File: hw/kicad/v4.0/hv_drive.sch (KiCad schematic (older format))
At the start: 24 parts, among them P6 CONN_01X02, P8 CONN_01X03, U12 IRAM256a

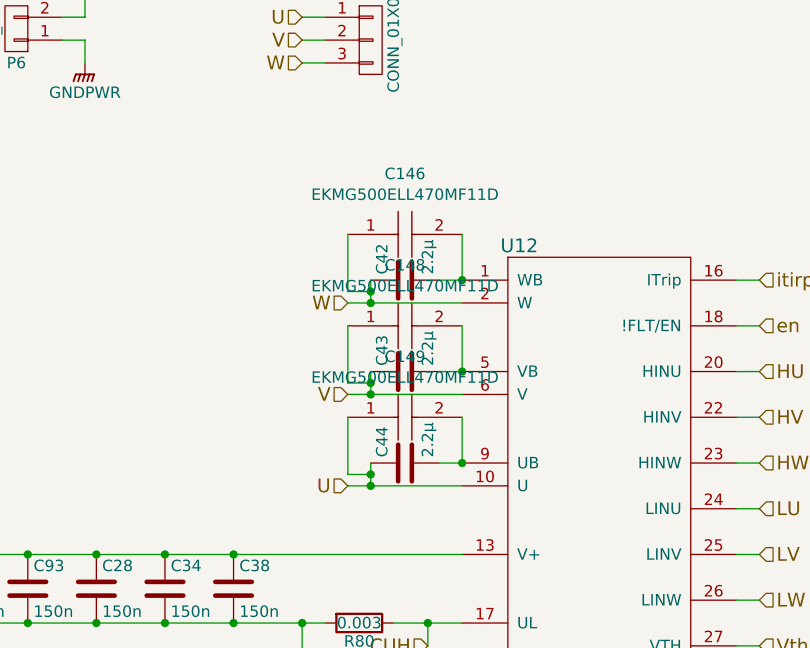
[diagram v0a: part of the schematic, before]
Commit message: added IKCM30F60GD
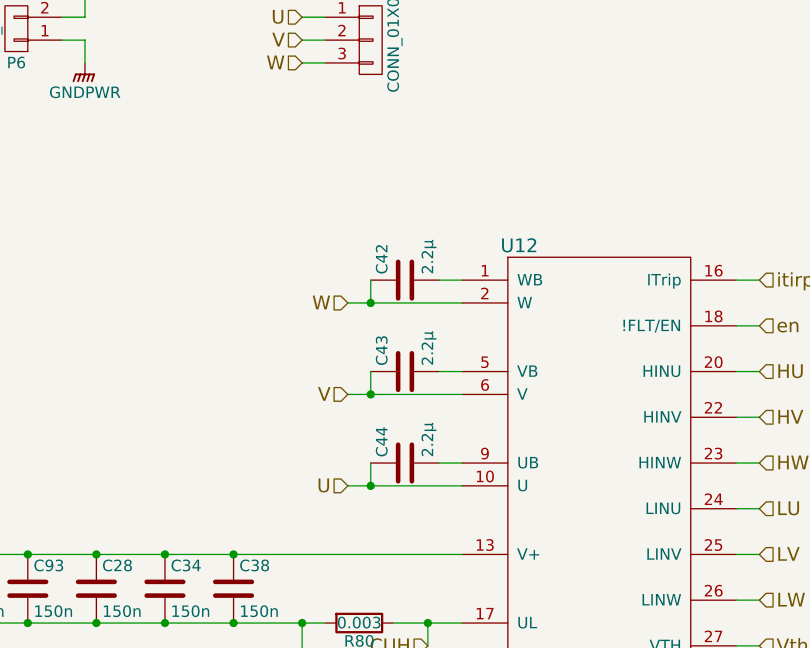
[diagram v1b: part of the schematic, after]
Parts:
- removed C146, C148, C149: EKMG500ELL470MF11D, SamacSys_Parts:CAPPRD250W60D680H1250, symbol SamacSys_Parts:EKMG500ELL470MF11D
- C42, C43, C44: footprint stmbl:C_1206 -> stmbl:C_0603
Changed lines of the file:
@@
 EESchema Schematic File Version 4
-EELAYER 30 0
+LIBS:stmbl_4.0-cache
+EELAYER 26 0
 EELAYER END
 $Descr A4 11693 8268
@@
 F 0 "C42" H 5625 3150 50  0000 L CNN
 F 1 "2.2µ" H 5625 2950 50  0000 L CNN
-F 2 "stmbl:C_1206" H 5638 2900 30  0001 C CNN
+F 2 "stmbl:C_0603" H 5638 2900 30  0001 C CNN
 F 3 "" H 5600 3050 60  0000 C CNN
 F 4 "" H 5600 3050 60  0001 C CNN "InternalName"
@@
 F 0 "C43" H 5625 3550 50  0000 L CNN
 F 1 "2.2µ" H 5625 3350 50  0000 L CNN
-F 2 "stmbl:C_1206" H 5638 3300 30  0001 C CNN
+F 2 "stmbl:C_0603" H 5638 3300 30  0001 C CNN
 F 3 "" H 5600 3450 60  0000 C CNN
 F 4 "" H 5600 3450 60  0001 C CNN "InternalName"
@@
 	5350 3550 5450 3550
 Wire Wire Line
-	5450 3450 5450 3500
+	5450 3450 5450 3550
 Connection ~ 5450 3550
 $Comp
@@
 F 0 "C44" H 5625 3950 50  0000 L CNN
 F 1 "2.2µ" H 5625 3750 50  0000 L CNN
-F 2 "stmbl:C_1206" H 5638 3700 30  0001 C CNN
+F 2 "stmbl:C_0603" H 5638 3700 30  0001 C CNN
 F 3 "" H 5600 3850 60  0000 C CNN
 F 4 "" H 5600 3850 60  0001 C CNN "InternalName"
@@
 $EndComp
 Wire Wire Line
+	5850 3850 5750 3850
+Wire Wire Line
 	5350 3950 5450 3950
 Wire Wire Line
-	5450 3850 5450 3900
+	5450 3850 5450 3950
 Connection ~ 5450 3950
 $Comp
@@
 	7800 4550 7900 4550
 Wire Wire Line
-	5450 3050 5450 3100
+	5450 3050 5450 3150
 Wire Wire Line
 	5150 4550 5150 4750
@@
 Wire Wire Line
 	8100 4750 8400 4750
-$Comp
-L SamacSys_Parts:EKMG500ELL470MF11D C146
-U 1 1 5DF898C9
-P 5350 2850
-F 0 "C146" H 5600 3115 50  0000 C CNN
-F 1 "EKMG500ELL470MF11D" H 5600 3024 50  0000 C CNN
-F 2 "SamacSys_Parts:CAPPRD250W60D680H1250" H 5700 2900 50  0001 L CNN
-F 3 "https://componentsearchengine.com/Datasheets/1/EKMG500ELL470MF11D.pdf" H 5700 2800 50  0001 L CNN
-F 4 "UNITED CHEMI-CON - EKMG500ELL470MF11D - ALUMINUM ELECTROLYTIC CAPACITOR 47UF, 50V, 20%, RADIAL" H 5700 2700 50  0001 L CNN "Description"
-F 5 "12.5" H 5700 2600 50  0001 L CNN "Height"
-F 6 "661-EKMGG500ELL470MF" H 5700 2500 50  0001 L CNN "Mouser Part Number"
-F 7 "https://www.mouser.com/Search/Refine.aspx?Keyword=661-EKMGG500ELL470MF" H 5700 2400 50  0001 L CNN "Mouser Price/Stock"
-F 8 "United Chemi-Con" H 5700 2300 50  0001 L CNN "Manufacturer_Name"
-F 9 "EKMG500ELL470MF11D" H 5700 2200 50  0001 L CNN "Manufacturer_Part_Number"
-	1    5350 2850
-	1    0    0    -1
-$EndComp
-$Comp
-L SamacSys_Parts:EKMG500ELL470MF11D C148
-U 1 1 5DF8F912
-P 5350 3250
-F 0 "C148" H 5600 3515 50  0000 C CNN
-F 1 "EKMG500ELL470MF11D" H 5600 3424 50  0000 C CNN
-F 2 "SamacSys_Parts:CAPPRD250W60D680H1250" H 5700 3300 50  0001 L CNN
-F 3 "https://componentsearchengine.com/Datasheets/1/EKMG500ELL470MF11D.pdf" H 5700 3200 50  0001 L CNN
-F 4 "UNITED CHEMI-CON - EKMG500ELL470MF11D - ALUMINUM ELECTROLYTIC CAPACITOR 47UF, 50V, 20%, RADIAL" H 5700 3100 50  0001 L CNN "Description"
-F 5 "12.5" H 5700 3000 50  0001 L CNN "Height"
-F 6 "661-EKMGG500ELL470MF" H 5700 2900 50  0001 L CNN "Mouser Part Number"
-F 7 "https://www.mouser.com/Search/Refine.aspx?Keyword=661-EKMGG500ELL470MF" H 5700 2800 50  0001 L CNN "Mouser Price/Stock"
-F 8 "United Chemi-Con" H 5700 2700 50  0001 L CNN "Manufacturer_Name"
-F 9 "EKMG500ELL470MF11D" H 5700 2600 50  0001 L CNN "Manufacturer_Part_Number"
-	1    5350 3250
-	1    0    0    -1
-$EndComp
-$Comp
-L SamacSys_Parts:EKMG500ELL470MF11D C149
-U 1 1 5DF91ED9
-P 5350 3650
-F 0 "C149" H 5600 3915 50  0000 C CNN
-F 1 "EKMG500ELL470MF11D" H 5600 3824 50  0000 C CNN
-F 2 "SamacSys_Parts:CAPPRD250W60D680H1250" H 5700 3700 50  0001 L CNN
-F 3 "https://componentsearchengine.com/Datasheets/1/EKMG500ELL470MF11D.pdf" H 5700 3600 50  0001 L CNN
-F 4 "UNITED CHEMI-CON - EKMG500ELL470MF11D - ALUMINUM ELECTROLYTIC CAPACITOR 47UF, 50V, 20%, RADIAL" H 5700 3500 50  0001 L CNN "Description"
-F 5 "12.5" H 5700 3400 50  0001 L CNN "Height"
-F 6 "661-EKMGG500ELL470MF" H 5700 3300 50  0001 L CNN "Mouser Part Number"
-F 7 "https://www.mouser.com/Search/Refine.aspx?Keyword=661-EKMGG500ELL470MF" H 5700 3200 50  0001 L CNN "Mouser Price/Stock"
-F 8 "United Chemi-Con" H 5700 3100 50  0001 L CNN "Manufacturer_Name"
-F 9 "EKMG500ELL470MF11D" H 5700 3000 50  0001 L CNN "Manufacturer_Part_Number"
-	1    5350 3650
-	1    0    0    -1
-$EndComp
-Wire Wire Line
-	5850 3650 5850 3850
-Connection ~ 5850 3850
-Wire Wire Line
-	5850 3250 5850 3450
-Wire Wire Line
-	5750 3850 5850 3850
-Connection ~ 5850 3450
-Wire Wire Line
-	5850 2850 5850 3050
-Connection ~ 5850 3050
-Wire Wire Line
-	5350 2850 5350 3100
-Wire Wire Line
-	5350 3100 5450 3100
-Connection ~ 5450 3100
-Wire Wire Line
-	5450 3100 5450 3150
-Wire Wire Line
-	5350 3250 5350 3500
-Wire Wire Line
-	5350 3500 5450 3500
-Connection ~ 5450 3500
-Wire Wire Line
-	5450 3500 5450 3550
-Wire Wire Line
-	5350 3650 5350 3900
-Wire Wire Line
-	5350 3900 5450 3900
-Connection ~ 5450 3900
-Wire Wire Line
-	5450 3900 5450 3950
 $EndSCHEMATC

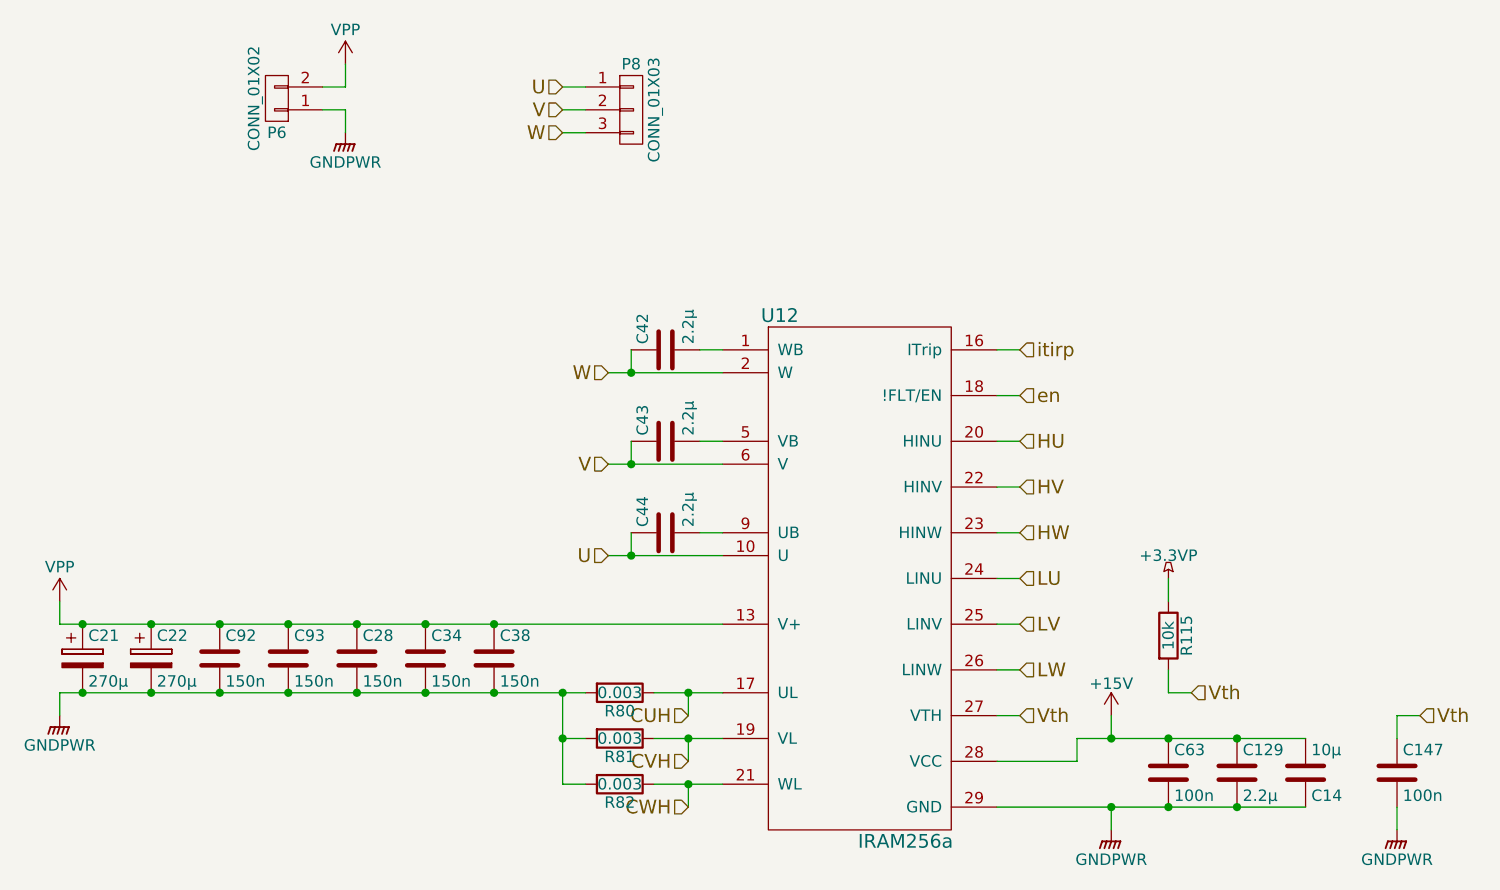
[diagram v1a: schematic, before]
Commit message: schematic update
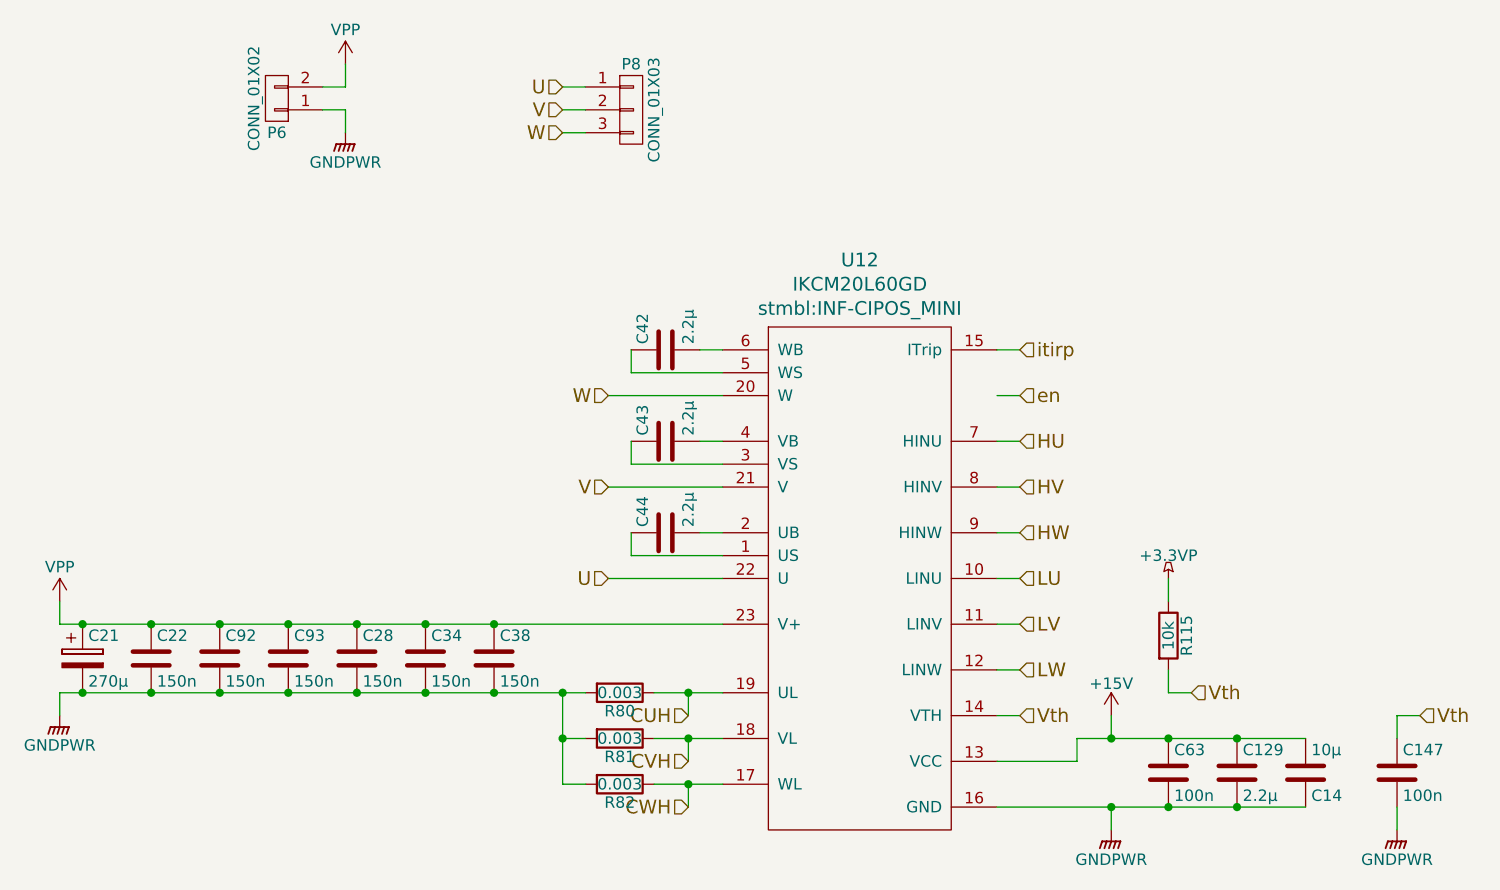
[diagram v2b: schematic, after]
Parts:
- removed C22: 270µ, stmbl:C_Radial_D26_L45_P10, symbol stmbl:CP
- removed U12: IRAM256a, stmbl:IRAM256, symbol stmbl:IRAM256a
- added C22: 150n, stmbl:C_1808, symbol stmbl:C
- added U12: IKCM20L60GD, stmbl:INF-CIPOS_MINI, symbol stmbl:IKCM20L60GD
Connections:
- net +15V: now also U12.13 (VCC)
- net CUH: now also U12.19 (UL)
- net CVH: now also U12.18 (VL)
- net CWH: now also U12.17 (WL)
- net GNDPWR: now also C22.2, U12.16 (GND)
- net HU: now also U12.7 (HINU)
- net HV: now also U12.8 (HINV)
- net HW: now also U12.9 (HINW)
- net LU: now also U12.10 (LINU)
- net LV: now also U12.11 (LINV)
- net LW: now also U12.12 (LINW)
- net U: now also U12.22 (U); no longer C44.1
- net V: now also U12.21 (V); no longer C43.1
- net VPP: now also C22.1, U12.23 (V+)
- net Vth: now also U12.14 (VTH)
- net W: now also U12.20 (W); no longer C42.1
- net itirp: now also U12.15 (ITrip)
- net at C42.2: now also U12.6 (WB)
- net at C43.2: now also U12.4 (VB)
- net at C44.2: now also U12.2 (UB)
- new net: C42.1, U12.5 (WS)
- new net: C43.1, U12.3 (VS)
- new net: C44.1, U12.1 (US)
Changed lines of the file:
@@
 EESchema Schematic File Version 4
-LIBS:stmbl_4.0-cache
-EELAYER 26 0
+EELAYER 30 0
 EELAYER END
 $Descr A4 11693 8268
@@
 $EndComp
 $Comp
-L stmbl:CP C22
-U 1 1 56590CD1
-P 3350 4400
-F 0 "C22" H 3375 4500 50  0000 L CNN
-F 1 "270µ" H 3375 4300 50  0000 L CNN
-F 2 "stmbl:C_Radial_D26_L45_P10" H 3388 4250 30  0001 C CNN
-F 3 "" H 3350 4400 60  0000 C CNN
-F 4 "" H 3350 4400 60  0001 C CNN "InternalName"
-F 5 "ESMR401VSN271MQ30S" H 3350 4400 60  0001 C CNN "Manufacturer No"
-F 6 "400V" H 3350 4400 60  0001 C CNN "Voltage"
-F 7 "" H 3350 4400 60  0001 C CNN "Source"
-F 8 "" H 3350 4400 60  0001 C CNN "Tolerance"
-F 9 "" H 0   0   50  0001 C CNN "Description"
-F 10 "United Chemi-Con" H 0   0   50  0001 C CNN "Manufacturer"
-	1    3350 4400
-	1    0    0    -1
-$EndComp
-$Comp
 L stmbl:C C28
 U 1 1 56590D2C
@@
 Connection ~ 4550 4550
 Connection ~ 4250 4550
-Connection ~ 3350 4550
-Connection ~ 3350 4250
 Connection ~ 4250 4250
 Connection ~ 4550 4250
@@
 Wire Wire Line
 	5850 3050 5750 3050
-Wire Wire Line
-	5350 3150 5450 3150
-Text HLabel 5350 3150 0    60   Input ~ 0
-W
-Text HLabel 5350 3550 0    60   Input ~ 0
-V
-Text HLabel 5350 3950 0    60   Input ~ 0
-U
 Connection ~ 3050 4250
-Connection ~ 5450 3150
 Text HLabel 5150 1900 0    60   Input ~ 0
 U
@@
 $EndComp
 $Comp
-L stmbl:IRAM256a U12
-U 1 1 5668DD3B
-P 6450 4050
-F 0 "U12" H 6100 5200 60  0000 C CNN
-F 1 "IRAM256a" H 6650 2900 60  0000 C CNN
-F 2 "stmbl:IRAM256" H 6450 4050 60  0001 C CNN
-F 3 "" H 6450 4050 60  0000 C CNN
-F 4 "IRAM256-2067A2" H 6450 4050 50  0001 C CNN "Manufacturer No"
-F 5 "" H 6450 4050 50  0001 C CNN "Voltage"
-F 6 "" H 6450 4050 50  0001 C CNN "Source"
-F 7 "" H 6450 4050 60  0001 C CNN "InternalName"
-F 8 "" H 6450 4050 60  0001 C CNN "Tolerance"
-F 9 "" H 0   0   50  0001 C CNN "Description"
-F 10 "Infineon" H 0   0   50  0001 C CNN "Manufacturer"
-	1    6450 4050
-	1    0    0    -1
-$EndComp
-$Comp
 L stmbl:C C43
 U 1 1 5668E03D
@@
 	5850 3450 5750 3450
 Wire Wire Line
-	5350 3550 5450 3550
-Wire Wire Line
 	5450 3450 5450 3550
-Connection ~ 5450 3550
 $Comp
 L stmbl:C C44
@@
 	5850 3850 5750 3850
 Wire Wire Line
-	5350 3950 5450 3950
-Wire Wire Line
 	5450 3850 5450 3950
-Connection ~ 5450 3950
 $Comp
 L stmbl:R R80
@@
 	4250 4550 4550 4550
 Wire Wire Line
+	4250 4250 4550 4250
+Wire Wire Line
+	4550 4250 4850 4250
+Wire Wire Line
+	5150 4550 5250 4550
+Wire Wire Line
+	5450 3150 5850 3150
+Wire Wire Line
+	5450 3550 5850 3550
+Wire Wire Line
+	5450 3950 5850 3950
+Wire Wire Line
+	5700 4550 5850 4550
+Wire Wire Line
+	5700 4750 5850 4750
+Wire Wire Line
+	5700 4950 5850 4950
+Wire Wire Line
+	7550 5050 7800 5050
+Wire Wire Line
+	7550 4750 7800 4750
+Wire Wire Line
+	5150 4750 5150 4950
+Wire Wire Line
+	3650 4550 3950 4550
+Wire Wire Line
+	3950 4550 4250 4550
+Wire Wire Line
+	3950 4250 4250 4250
+Wire Wire Line
+	3650 4250 3950 4250
+Wire Wire Line
+	4850 4550 5150 4550
+Wire Wire Line
+	4850 4250 5850 4250
+Wire Wire Line
+	7800 5050 8100 5050
+Wire Wire Line
+	7800 4750 8100 4750
+Wire Wire Line
+	8100 5050 8400 5050
+Wire Wire Line
+	8100 4750 8400 4750
+$Comp
+L stmbl:IKCM20L60GD U12
+U 1 1 5EC2EF5C
+P 6450 4050
+F 0 "U12" H 6450 5443 60  0000 C CNN
+F 1 "IKCM20L60GD" H 6450 5337 60  0000 C CNN
+F 2 "stmbl:INF-CIPOS_MINI" H 6450 5231 60  0000 C CNN
+F 3 "" H 6450 4050 60  0000 C CNN
+	1    6450 4050
+	1    0    0    -1
+$EndComp
+Wire Wire Line
+	5350 3250 5850 3250
+Wire Wire Line
+	5350 3650 5850 3650
+Wire Wire Line
+	5350 4050 5850 4050
+Text HLabel 5350 4050 0    60   Input ~ 0
+U
+Text HLabel 5350 3650 0    60   Input ~ 0
+V
+Text HLabel 5350 3250 0    60   Input ~ 0
+W
+Wire Wire Line
+	3050 4550 3350 4550
+Wire Wire Line
+	3050 4250 3350 4250
+$Comp
+L stmbl:C C22
+U 1 1 5EC3BB72
+P 3350 4400
+F 0 "C22" H 3375 4500 50  0000 L CNN
+F 1 "150n" H 3375 4300 50  0000 L CNN
+F 2 "stmbl:C_1808" H 3388 4250 30  0001 C CNN
+F 3 "" H 3350 4400 60  0000 C CNN
+F 4 "" H 3350 4400 60  0001 C CNN "InternalName"
+F 5 "C1808W154KCRACTU" H 3350 4400 60  0001 C CNN "Manufacturer No"
+F 6 "500V" H 3350 4400 60  0001 C CNN "Voltage"
+F 7 "" H 3350 4400 60  0001 C CNN "Source"
+F 8 "X7R" H 3350 4400 60  0001 C CNN "Tolerance"
+F 9 "" H -300 0   50  0001 C CNN "Description"
+F 10 "KEMET" H -300 0   50  0001 C CNN "Manufacturer"
+	1    3350 4400
+	1    0    0    -1
+$EndComp
+Connection ~ 3350 4250
+Wire Wire Line
+	3350 4250 3650 4250
+Connection ~ 3350 4550
+Wire Wire Line
 	3350 4550 3650 4550
-Wire Wire Line
-	3350 4250 3650 4250
-Wire Wire Line
-	4250 4250 4550 4250
-Wire Wire Line
-	4550 4250 4850 4250
-Wire Wire Line
-	5150 4550 5250 4550
-Wire Wire Line
-	3050 4250 3350 4250
-Wire Wire Line
-	5450 3150 5850 3150
-Wire Wire Line
-	5450 3550 5850 3550
-Wire Wire Line
-	5450 3950 5850 3950
-Wire Wire Line
-	5700 4550 5850 4550
-Wire Wire Line
-	5700 4750 5850 4750
-Wire Wire Line
-	5700 4950 5850 4950
-Wire Wire Line
-	3050 4550 3350 4550
-Wire Wire Line
-	7550 5050 7800 5050
-Wire Wire Line
-	7550 4750 7800 4750
-Wire Wire Line
-	5150 4750 5150 4950
-Wire Wire Line
-	3650 4550 3950 4550
-Wire Wire Line
-	3950 4550 4250 4550
-Wire Wire Line
-	3950 4250 4250 4250
-Wire Wire Line
-	3650 4250 3950 4250
-Wire Wire Line
-	4850 4550 5150 4550
-Wire Wire Line
-	4850 4250 5850 4250
-Wire Wire Line
-	7800 5050 8100 5050
-Wire Wire Line
-	7800 4750 8100 4750
-Wire Wire Line
-	8100 5050 8400 5050
-Wire Wire Line
-	8100 4750 8400 4750
 $EndSCHEMATC
